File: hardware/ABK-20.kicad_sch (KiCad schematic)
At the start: 52 parts, among them J1 CONN_01X04, J2 CONN_01X04, J3 CONN_02X03, J4 Con_3-5V, J5 USB_C_6P, J6 Sync_Jumper, SW1 SW_SPST, SW2 SW_Push, SW3 SW_SPDT_MSM, SW4 SW_Push, U1 ATTINY85-20SU, U2 PAM8002, U3 7805

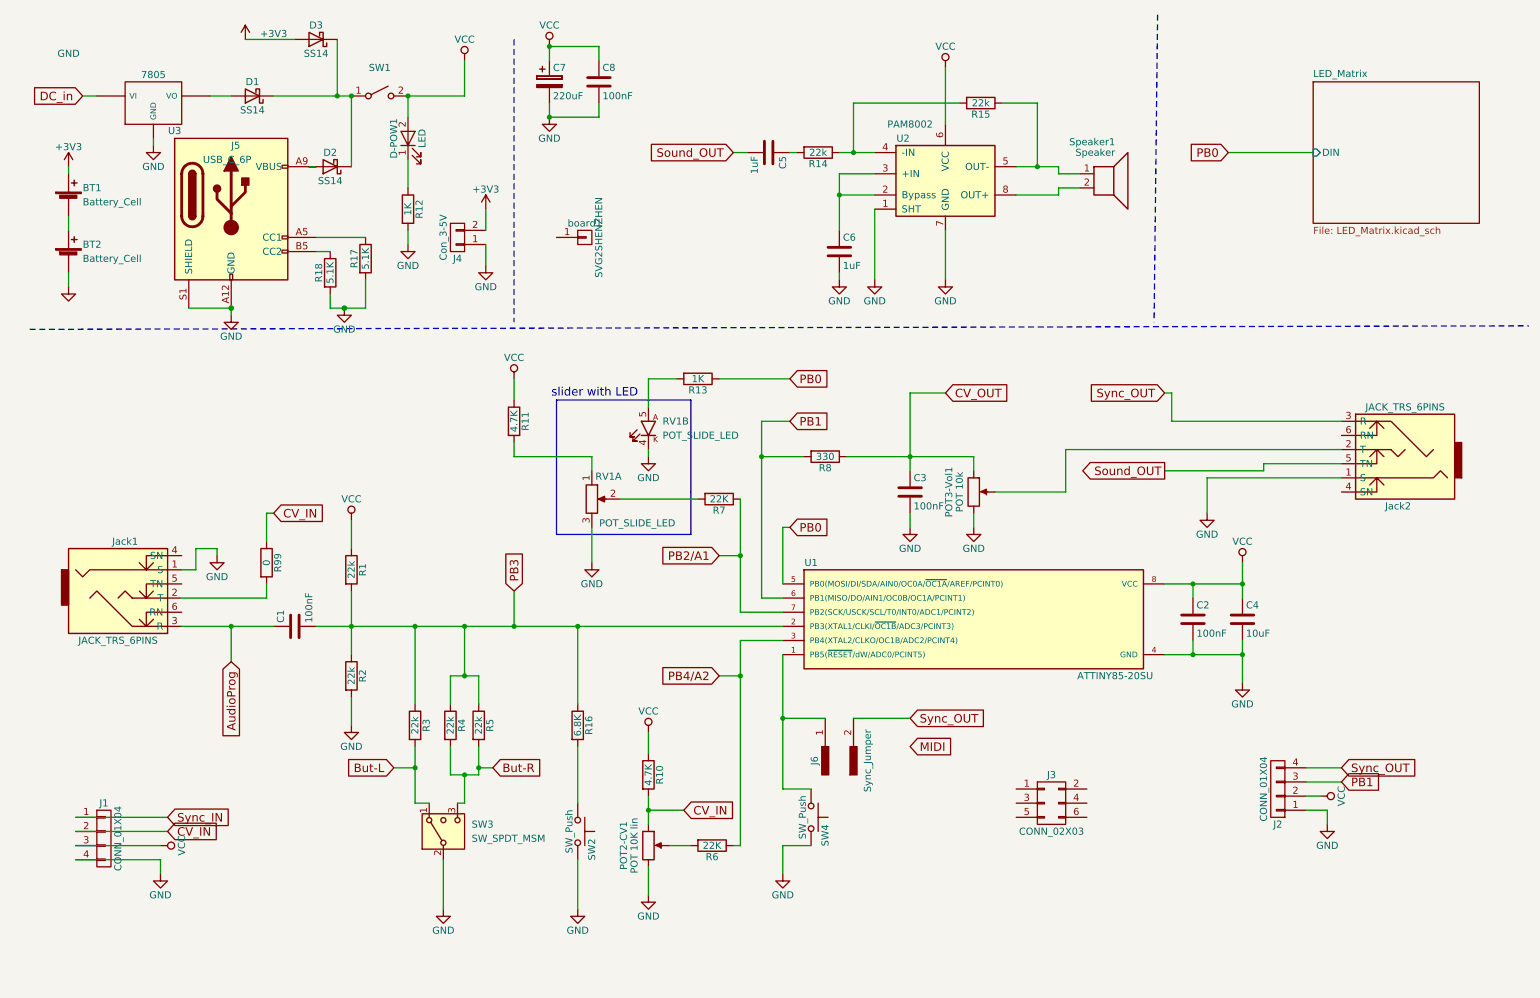
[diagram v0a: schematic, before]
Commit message: fix(pcb): flip components to F.Cu and correct horizontal audio jack 3D orientation
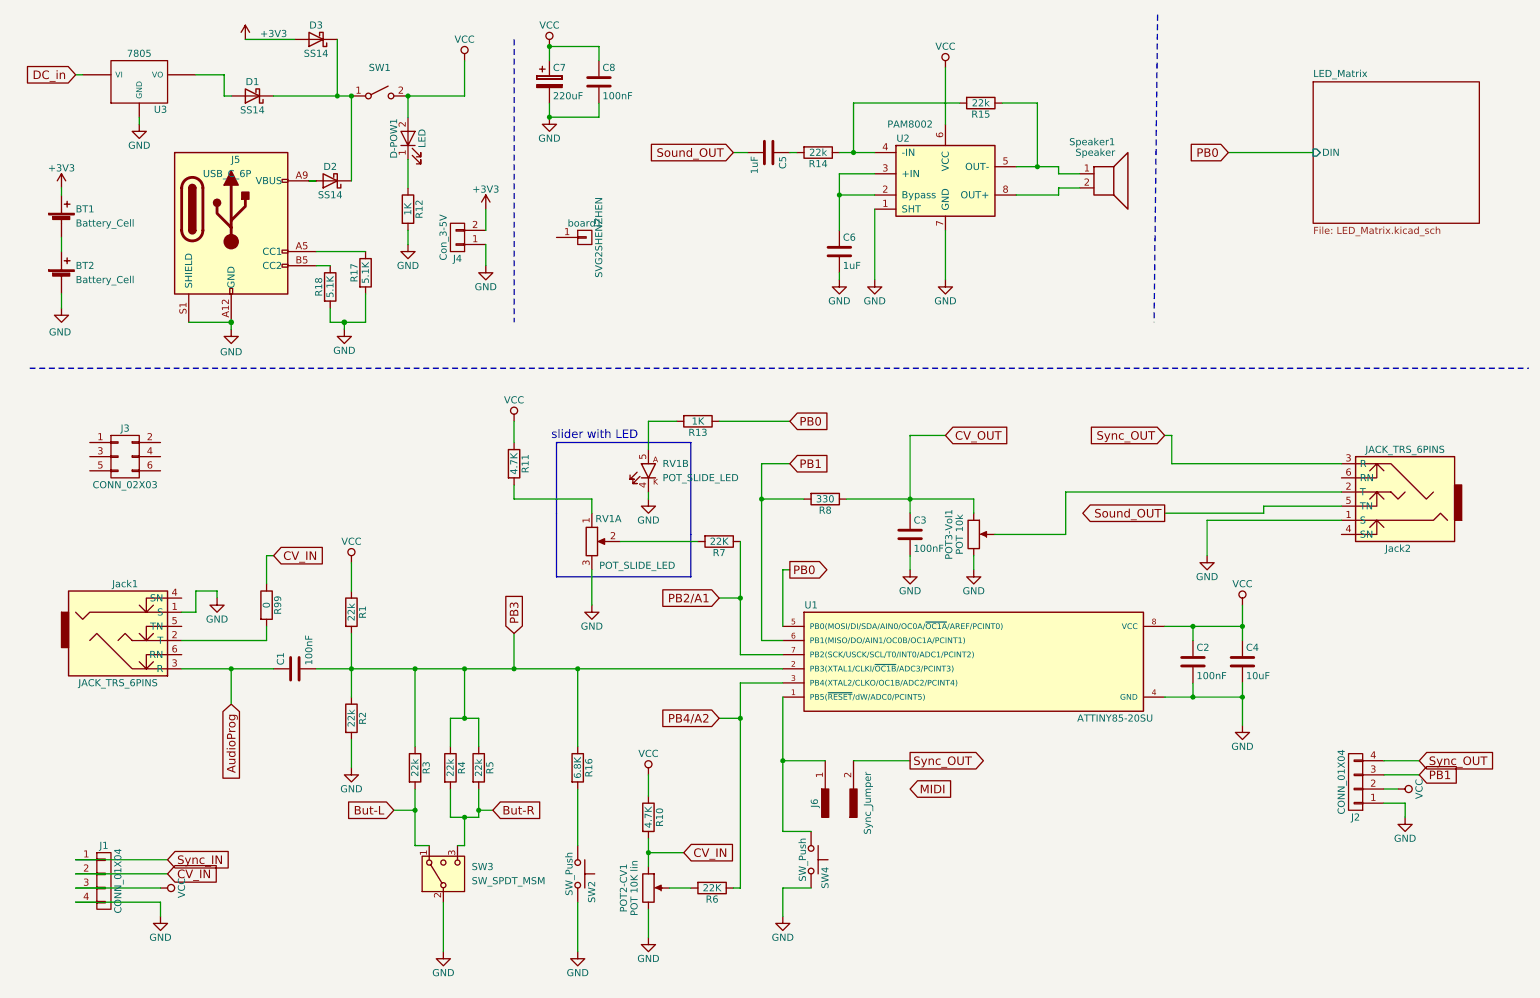
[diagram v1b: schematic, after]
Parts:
- RV1: footprint 8Bitmixtape_reworked:Potentiometer_Bourns_PTL20_Single_Slide_LED -> 8Bitmixtape_reworked:Potentiometer_Bourns_PTL30_Single_Slide_LED
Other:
- moved on the sheet: BT1, BT2, C1, C2, C3, C4, D2, J1, J2, J3, J5, J6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

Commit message: fix(pcb, footprints): shift Bourns slide pot right side pads +2.5mm in Y to match physical part
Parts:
- RV1: footprint 8Bitmixtape_reworked:Potentiometer_Bourns_PTL30_Single_Slide_LED -> 8Bitmixtape_reworked:Potentiometer_Bourns_PTL20_Single_Slide_LED
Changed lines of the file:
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@@
 			)
 		)
-		(property "Footprint" "8Bitmixtape_reworked:Potentiometer_Bourns_PTL30_Single_Slide_LED"
+		(property "Footprint" "8Bitmixtape_reworked:Potentiometer_Bourns_PTL20_Single_Slide_LED"
 			(at 124.46 96.52 0)
 			(effects
@@
 			)
 		)
-		(property "Footprint" "8Bitmixtape_reworked:Potentiometer_Bourns_PTL30_Single_Slide_LED"
+		(property "Footprint" "8Bitmixtape_reworked:Potentiometer_Bourns_PTL20_Single_Slide_LED"
 			(at 114.3 109.22 0)
 			(effects

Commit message: feat(hardware): add Highly KS01-BL-13 illuminated keypad button footprint and 3D model for SW2
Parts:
- SW2: footprint 8Bitmixtape_reworked:TACTILE-PTH_6mm_SMD -> 8Bitmixtape_reworked:SW_Push_Highly_KS01-BL-13
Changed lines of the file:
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@@
 			)
 		)
-		(property "Footprint" "8Bitmixtape_reworked:TACTILE-PTH_6mm_SMD"
+		(property "Footprint" "8Bitmixtape_reworked:SW_Push_Highly_KS01-BL-13"
 			(at 116.84 168.91 0)
 			(effects

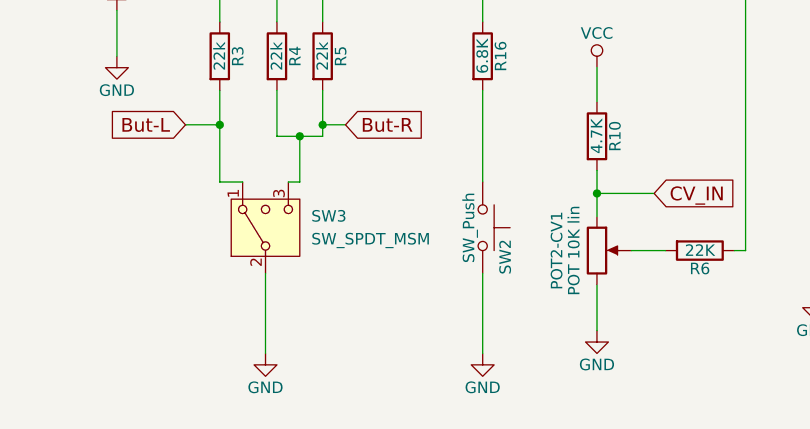
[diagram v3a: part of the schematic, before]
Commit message: Add 2-unit SW_Push_LED symbol for KS01-BL-13 with switch (Unit A) and bi-color LED (Unit B)
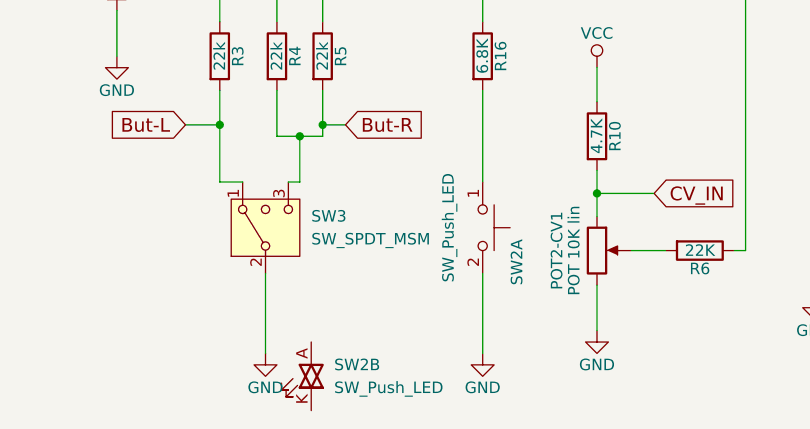
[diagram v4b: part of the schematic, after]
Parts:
- added unit 2 of SW2
- SW2: value SW_Push -> SW_Push_LED; symbol mixtape_schematics:SW_Push -> ABK-20-rescue:SW_Push_LED
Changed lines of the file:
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@@
 	)
 	(symbol
-		(lib_id "mixtape_schematics:SW_Push")
+		(lib_id "ABK-20-rescue:SW_Push_LED")
 		(at 111.76 168.91 270)
 		(unit 1)
@@
 		(dnp no)
 		(property "Reference" "SW2"
-			(at 114.3 170.18 0)
+			(at 115.57 170.18 0)
 			(effects
 				(font
@@
 			)
 		)
-		(property "Value" "SW_Push"
-			(at 110.236 168.91 0)
+		(property "Value" "SW_Push_LED"
+			(at 107.95 168.91 0)
 			(effects
 				(font
 					(size 1.27 1.27)
-				)
-			)
+				))
 		)
 		(property "Footprint" "8Bitmixtape_reworked:SW_Push_Highly_KS01-BL-13"
@@
 			)
 		)
-		(property "Datasheet" ""
+		(property "Datasheet" "https://www.tme.eu/Document/445b24673c2c7fe28e59716d9a77095b/KS01+series.pdf"
 			(at 116.84 168.91 0)
 			(effects
@@
 			)
 		)
-		(property "Description" ""
+		(property "Description" "Highly Electric KS01-BL-13 Illuminated Push Button (Unit A: Switch, Unit B: Bi-color LED)"
 			(at 111.76 168.91 0)
 			(effects
@@
 					(size 1.27 1.27)
 				)
+				(hide yes)
 			)
 		)
@@
 				)
 			)
+		)
+	)
+	(symbol
+		(lib_id "ABK-20-rescue:SW_Push_LED")
+		(at 92.71 185.42 0)
+		(unit 2)
+		(exclude_from_sim no)
+		(in_bom yes)
+		(on_board yes)
+		(dnp no)
+		(property "Reference" "SW2"
+			(at 95.25 184.15 0)
+			(effects
+				(font
+					(size 1.27 1.27)
+				)
+				(justify left)
+			)
+		)
+		(property "Value" "SW_Push_LED"
+			(at 95.25 186.69 0)
+			(effects
+				(font
+					(size 1.27 1.27)
+				)
+				(justify left)
+			)
+		)
+		(property "Footprint" "8Bitmixtape_reworked:SW_Push_Highly_KS01-BL-13"
+			(at 111.76 195.58 0)
+			(effects
+				(font
+					(size 1.27 1.27)
+				)
+				(hide yes)
+			)
+		)
+		(property "Datasheet" "https://www.tme.eu/Document/445b24673c2c7fe28e59716d9a77095b/KS01+series.pdf"
+			(at 111.76 195.58 0)
+			(effects
+				(font
+					(size 1.27 1.27)
+				)
+				(hide yes)
+			)
+		)
+		(property "Description" "Highly Electric KS01-BL-13 Illuminated Push Button (Unit A: Switch, Unit B: Bi-color LED)"
+			(at 111.76 195.58 0)
+			(effects
+				(font
+					(size 1.27 1.27)
+				)
+				(hide yes)
+			)
+		)
+		(pin "A"
+		)
+		(pin "K"
+		)
+		(instances
+			(project "ABK-20"
+				(path "/586acb5e-8acc-4ed8-b81f-7b15963d193b"
+					(reference "SW2")
+					(unit 2)
+				)
+			)

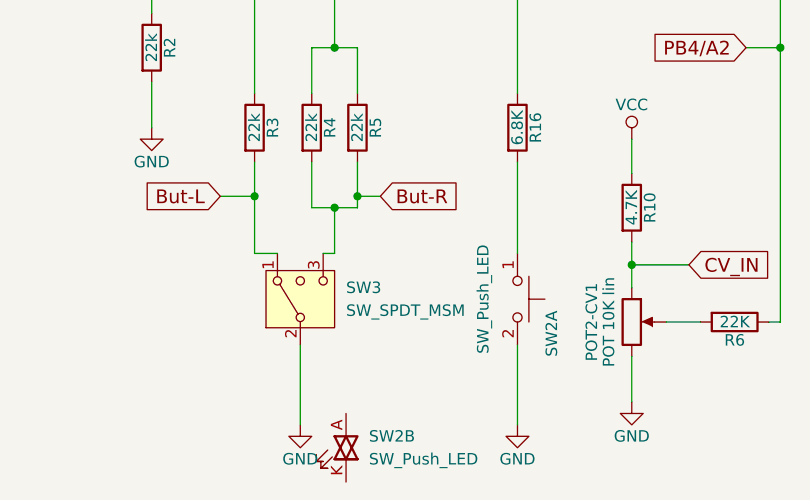
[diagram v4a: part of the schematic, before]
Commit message: style(schematic): rearrange SW2 push button and LED into grouped block
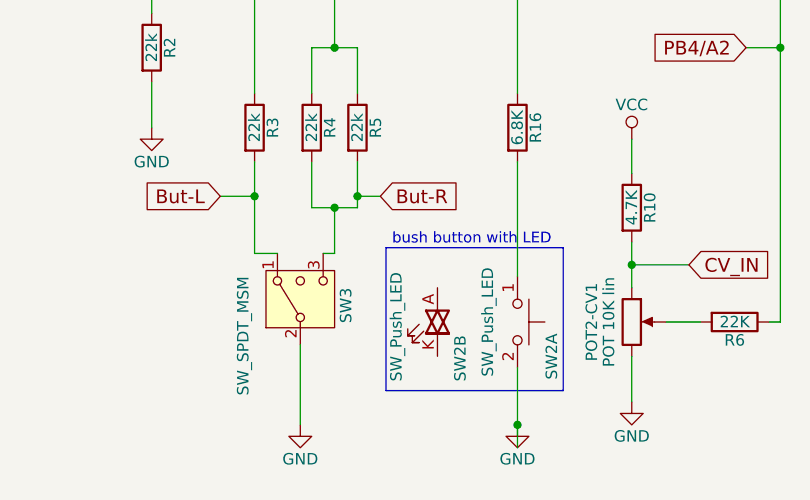
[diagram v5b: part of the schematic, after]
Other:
- note added: "bush button with LED"
- moved on the sheet: SW2A, SW2B
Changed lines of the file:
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@@
 		)
 	)
+	(text "bush button with LED"
+		(exclude_from_sim no)
+		(at 106.68 162.306 0)
+		(effects
+			(font
+				(size 1.2 1.2)
+			)
+		)
+	)
 	(junction
 		(at 82.55 157.48)
@@
 	)
 	(junction
+		(at 111.76 182.88)
+		(diameter 0)
+		(color 0 0 0 0)
+	)
+	(junction
 		(at 91.44 140.97)
 		(diameter 0)
@@
 	(wire
 		(pts
+			(xy 111.76 185.42) (xy 111.76 182.88)
+		)
+		(stroke
+			(width 0)
+			(type default)
+		)
+	)
+	(wire
+		(pts
 			(xy 21.59 166.37) (xy 38.1 166.37)
 		)
@@
 		)
 	)
+	(polyline
+		(pts
+			(xy 116.84 163.195) (xy 116.84 179.07)
+		)
+		(stroke
+			(width 0)
+			(type default)
+		)
+	)
 	(wire
 		(pts
@@
 	(polyline
 		(pts
+			(xy 97.155 163.195) (xy 116.84 163.195)
+		)
+		(stroke
+			(width 0)
+			(type default)
+		)
+	)
+	(polyline
+		(pts
 			(xy 107.95 104.14) (xy 107.95 91.44)
 		)
@@
 	(wire
 		(pts
-			(xy 111.76 173.99) (xy 111.76 182.88)
+			(xy 111.76 176.53) (xy 111.76 182.88)
 		)
 		(stroke
@@
 	(wire
 		(pts
-			(xy 111.76 153.67) (xy 111.76 163.83)
+			(xy 111.76 153.67) (xy 111.76 166.37)
 		)
 		(stroke
@@
 		)
 	)
+	(polyline
+		(pts
+			(xy 116.84 179.07) (xy 97.155 179.07)
+		)
+		(stroke
+			(width 0)
+			(type default)
+		)
+	)
 	(wire
 		(pts
@@
 		)
 	)
+	(polyline
+		(pts
+			(xy 97.155 179.07) (xy 97.155 163.195)
+		)
+		(stroke
+			(width 0)
+			(type default)
+		)
+	)
 	(wire
 		(pts
@@
 	(symbol
 		(lib_id "ABK-20-rescue:SW_Push_LED")
-		(at 111.76 168.91 270)
+		(at 111.76 171.45 270)
 		(unit 1)
 		(exclude_from_sim no)
@@
 		(dnp no)
 		(property "Reference" "SW2"
-			(at 115.57 170.18 0)
+			(at 115.57 172.72 0)
 			(effects
 				(font
@@
 		)
 		(property "Value" "SW_Push_LED"
-			(at 107.95 168.91 0)
+			(at 108.458 171.45 0)
 			(effects
 				(font
 					(size 1.27 1.27)
-				))
+				)
+			)
 		)
 		(property "Footprint" "8Bitmixtape_reworked:SW_Push_Highly_KS01-BL-13"
-			(at 116.84 168.91 0)
+			(at 116.84 171.45 0)
 			(effects
 				(font
@@
 		)
 		(property "Datasheet" "https://www.tme.eu/Document/445b24673c2c7fe28e59716d9a77095b/KS01+series.pdf"
-			(at 116.84 168.91 0)
+			(at 116.84 171.45 0)
 			(effects
 				(font
@@
 		)
 		(property "Description" "Highly Electric KS01-BL-13 Illuminated Push Button (Unit A: Switch, Unit B: Bi-color LED)"
-			(at 111.76 168.91 0)
+			(at 111.76 171.45 0)
 			(effects
 				(font
@@
 		(pin "2"
 		)
-		(instances
-			(project "ABK-20"
-				(path "/586acb5e-8acc-4ed8-b81f-7b15963d193b"
-					(reference "SW2")
-					(unit 1)
-				)
-			)
-		)
-	)
-	(symbol
-		(lib_id "ABK-20-rescue:SW_Push_LED")
-		(at 92.71 185.42 0)
-		(unit 2)
-		(exclude_from_sim no)
-		(in_bom yes)
-		(on_board yes)
-		(dnp no)
-		(property "Reference" "SW2"
-			(at 95.25 184.15 0)
-			(effects
-				(font
-					(size 1.27 1.27)
-				)
-				(justify left)
-			)
-		)
-		(property "Value" "SW_Push_LED"
-			(at 95.25 186.69 0)
-			(effects
-				(font
-					(size 1.27 1.27)
-				)
-				(justify left)
-			)
-		)
-		(property "Footprint" "8Bitmixtape_reworked:SW_Push_Highly_KS01-BL-13"
-			(at 111.76 195.58 0)
-			(effects
-				(font
-					(size 1.27 1.27)
-				)
-				(hide yes)
-			)
-		)
-		(property "Datasheet" "https://www.tme.eu/Document/445b24673c2c7fe28e59716d9a77095b/KS01+series.pdf"
-			(at 111.76 195.58 0)
-			(effects
-				(font
-					(size 1.27 1.27)
-				)
-				(hide yes)
-			)
-		)
-		(property "Description" "Highly Electric KS01-BL-13 Illuminated Push Button (Unit A: Switch, Unit B: Bi-color LED)"
-			(at 111.76 195.58 0)
-			(effects
-				(font
-					(size 1.27 1.27)
-				)
-				(hide yes)
-			)
+		(pin "K"
 		)
 		(pin "A"
 		)
-		(pin "K"
-		)
 		(instances
 			(project "ABK-20"
 				(path "/586acb5e-8acc-4ed8-b81f-7b15963d193b"
 					(reference "SW2")
-					(unit 2)
+					(unit 1)
 				)
 			)
@@
 		(on_board yes)
 		(dnp no)
-		(fields_autoplaced yes)
 		(property "Reference" "SW3"
-			(at 92.71 167.6399 90)
+			(at 92.71 167.6399 0)
 			(effects
 				(font
@@
 		)
 		(property "Value" "SW_SPDT_MSM"
-			(at 92.71 170.1799 90)
+			(at 81.28 166.37 0)
 			(effects
 				(font
@@
 				)
 			)
+		)
+	)
+	(symbol
+		(lib_id "ABK-20-rescue:SW_Push_LED")
+		(at 102.87 171.45 0)
+		(unit 2)
+		(exclude_from_sim no)
+		(in_bom yes)
+		(on_board yes)
+		(dnp no)
+		(property "Reference" "SW2"
+			(at 105.41 178.054 90)
+			(effects
+				(font
+					(size 1.27 1.27)
+				)
+				(justify left)
+			)
+		)
+		(property "Value" "SW_Push_LED"
+			(at 98.298 178.054 90)
+			(effects
+				(font
+					(size 1.27 1.27)
+				)
+				(justify left)
+			)
+		)
+		(property "Footprint" "8Bitmixtape_reworked:SW_Push_Highly_KS01-BL-13"
+			(at 121.92 181.61 0)
+			(effects
+				(font
+					(size 1.27 1.27)
+				)
+				(hide yes)
+			)
+		)
+		(property "Datasheet" "https://www.tme.eu/Document/445b24673c2c7fe28e59716d9a77095b/KS01+series.pdf"
+			(at 121.92 181.61 0)
+			(effects
+				(font
+					(size 1.27 1.27)
+				)
+				(hide yes)
+			)
+		)
+		(property "Description" "Highly Electric KS01-BL-13 Illuminated Push Button (Unit A: Switch, Unit B: Bi-color LED)"
+			(at 121.92 181.61 0)
+			(effects
+				(font
+					(size 1.27 1.27)
+				)
+				(hide yes)
+			)
+		)
+		(pin "A"
+		)
+		(pin "K"
+		)
+		(pin "1"
+		)
+		(pin "2"
+		)
+		(instances
+			(project "ABK-20"
+				(path "/586acb5e-8acc-4ed8-b81f-7b15963d193b"
+					(reference "SW2")
+					(unit 2)
+				)
+			)

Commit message: feat(3d-models): add recessed travel slit to Bourns PTL20/PTL30 slide pot models
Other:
- note added: "push button with LED"
- note removed: "bush button with LED"
- moved on the sheet: C1, R1, R2, R3, R4, R5, R99, SW3, SW4

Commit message: feat(pcb): finalize 75x80 component placement, self-contained 3D models, and variant showcase
- Place all core components on 75x80 mm board outline: 5x4 NeoPixel matrix, ATtiny85 DIP socket, Bourns slide pot, thumbwheel pot, illuminated RV09 pot, toggle switch, jacks, buttons, and side headers
- Create self-contained local 3D VRML library in hardware/3d_models/ with all project models bundled
- Add ABK-20_showcase_variants.kicad_pcb as standalone comparison showroom
- Fix pin numbering on 7805 voltage regulator (U3) and potentiometer mounting tabs (MP/L)
- Clean up jumper footprints and synchronize schematic assignments
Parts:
- J6: footprint 8Bitmixtape_reworked:Sync_jumper -> 8Bitmixtape_reworked:Sync_jumper_small
- Jack1, Jack2: footprint 8Bitmixtape_reworked:AUDIO-Jack_3.5mm_5Pin -> 8Bitmixtape_reworked:AUDIO-Jack_3.5mm_PJ-317
- POT2-CV1: footprint 8Bitmixtape_reworked:Potentiometer_backPads_noHole -> 8Bitmixtape_reworked:Potentiometer_RV09_Vertical_ClearShaft
- SW3: footprint 8Bitmixtape_reworked:SWITCH-SPDT_KIT -> 8Bitmixtape_reworked:SW_Toggle_SPDT_MTS-102
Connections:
- net DC_in: now also U3.1 (VI); no longer U3.VI
- net GND: now also U3.2 (GND); no longer U3.GND
- net at D1.2 (A): now also U3.3 (VO); no longer U3.VO
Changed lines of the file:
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@@
 			)
 		)
-		(property "Footprint" "8Bitmixtape_reworked:Potentiometer_backPads_noHole"
+		(property "Footprint" "8Bitmixtape_reworked:Potentiometer_RV09_Vertical_ClearShaft"
 			(at 124.46 171.45 0)
 			(effects
@@
 			)
 		)
-		(property "Footprint" "8Bitmixtape_reworked:AUDIO-Jack_3.5mm_5Pin"
+		(property "Footprint" "8Bitmixtape_reworked:AUDIO-Jack_3.5mm_PJ-317"
 			(at 256.54 96.52 0)
 			(effects
@@
 			)
 		)
-		(property "Footprint" "8Bitmixtape_reworked:AUDIO-Jack_3.5mm_5Pin"
+		(property "Footprint" "8Bitmixtape_reworked:AUDIO-Jack_3.5mm_PJ-317"
 			(at 33.02 130.81 0)
 			(effects
@@
 			)
 		)
-		(property "Footprint" "8Bitmixtape_reworked:Sync_jumper"
+		(property "Footprint" "8Bitmixtape_reworked:Sync_jumper_small"
 			(at 156.21 156.21 0)
 			(effects
@@
 			)
 		)
-		(pin "VI"
+		(pin "1"
 		)
-		(pin "GND"
+		(pin "2"
 		)
-		(pin "VO"
+		(pin "3"
 		)
 		(instances
@@
 			)
 		)
-		(property "Footprint" "8Bitmixtape_reworked:SWITCH-SPDT_KIT"
+		(property "Footprint" "8Bitmixtape_reworked:SW_Toggle_SPDT_MTS-102"
 			(at 69.85 182.88 0)
 			(effects
